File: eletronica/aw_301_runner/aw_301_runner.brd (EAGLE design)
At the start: 100 x 80 mm, 9 parts, among them IC1 AT90S2313P, Q1 4 Mhz

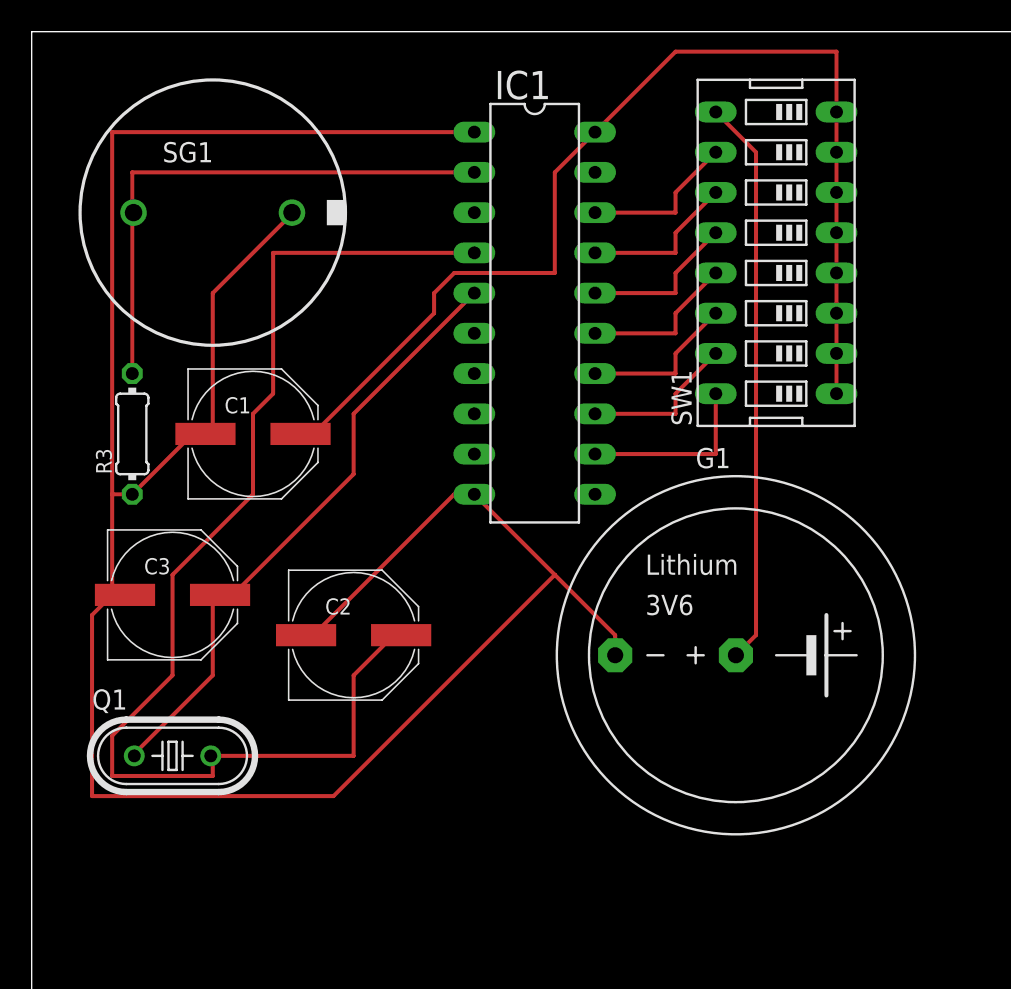
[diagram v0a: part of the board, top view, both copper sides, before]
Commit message: 
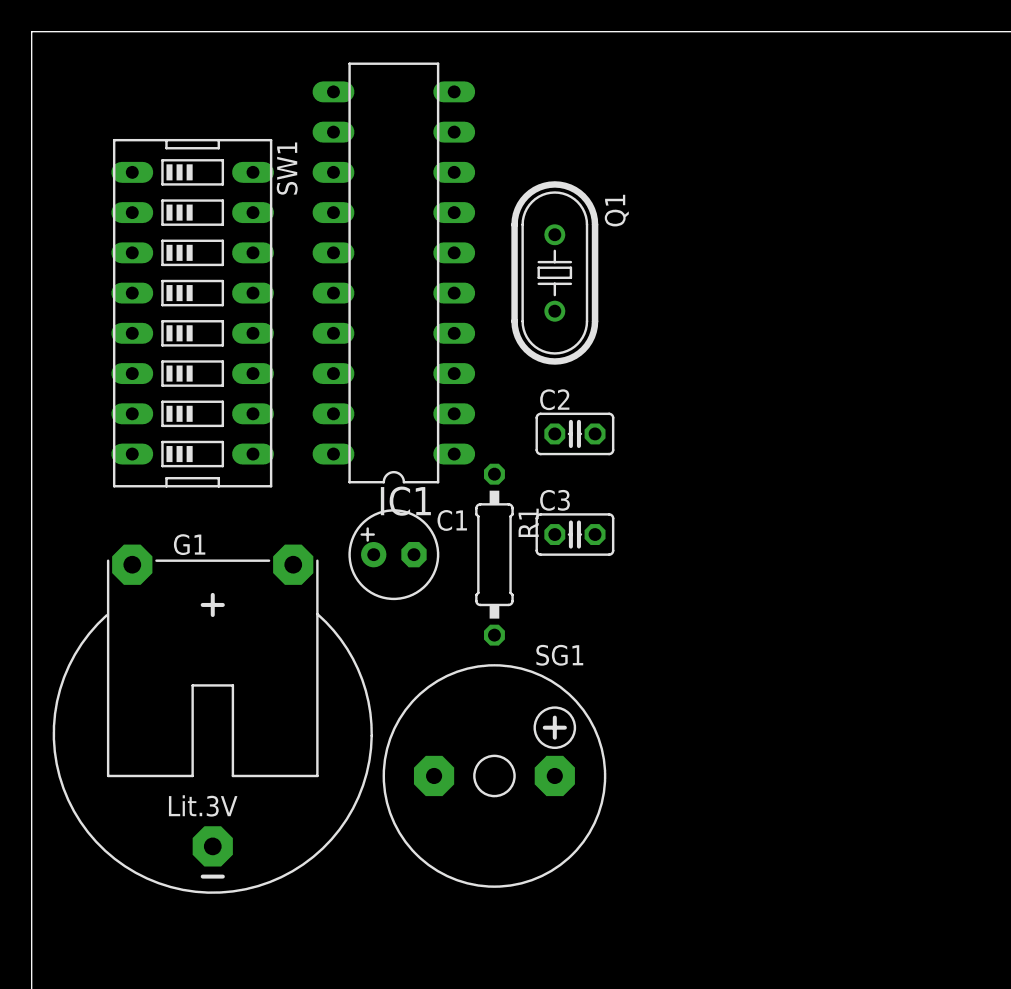
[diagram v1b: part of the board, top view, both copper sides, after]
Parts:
- removed R3: 1M, resistor:0204/7
- added R1: 1M, rcl:0207/10
- C1: device resistor:PANASONIC_E -> resistor:E2,5-6
- C2, C3: device resistor:PANASONIC_E -> rcl:C025-025X050
- G1: value SL340P -> CR2032H; device battery:SL-340/P3.6V -> battery:CR2032H
- Q1: value 4 Mhz -> (none); device crystal:HC49U-V -> crystal:HC49U70
- SG1: value EFBAA40D101 -> F/CM12P; device buzzer:EFBAA40D101 -> buzzer:F/CM12P
- moved SG1 39.8 mm to (29.2, 33.0)
- moved Q1 38.9 mm to (33.0, 64.8), turned to 270 degrees
- moved SW1 37.0 mm to (10.2, 62.2), turned to 270 degrees
- moved G1 33.4 mm to (11.4, 35.6)
- moved C3 25.7 mm to (34.3, 48.3)
- moved C2 18.9 mm to (34.3, 54.6)
- moved C1 11.7 mm to (22.9, 47.0)
- moved IC1 9.25 mm to (22.9, 64.8), turned to 90 degrees
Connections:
- net N$2: now also C2.2; no longer C2.+
- net N$3: now also C3.2; no longer C3.+
- net N$6: now also R1.2, SG1.+; no longer R3.2, SG1.1
- net N$7: now also C2.1, C3.1, R1.1, SG1.-; no longer C2.-, C3.-, R3.1, SG1.2
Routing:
- net N$7: track 153.3 -> 0.00 mm
- net N$2: track 75.7 -> 0.00 mm
- net N$5: track 69.9 -> 0.00 mm
- net N$3: track 39.0 -> 0.00 mm
- net N$1: track 35.9 -> 0.00 mm
- net N$6: track 34.4 -> 0.00 mm
- net N$8: track 11.4 -> 0.00 mm
- net N$14: track 9.94 -> 0.00 mm
- net N$12: track 9.94 -> 0.00 mm
- net N$9: track 9.94 -> 0.00 mm
- net N$11: track 9.94 -> 0.00 mm
- net N$10: track 9.94 -> 0.00 mm
- net N$13: track 9.94 -> 0.00 mm

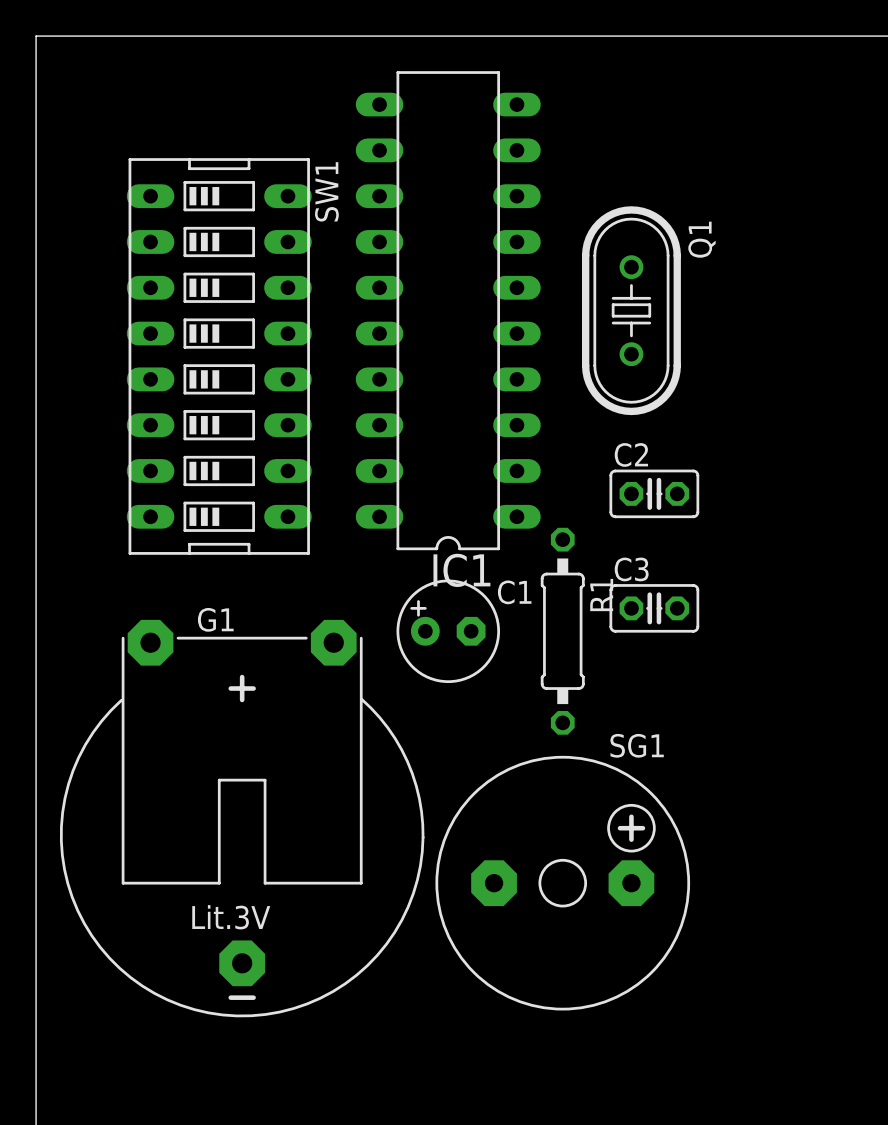
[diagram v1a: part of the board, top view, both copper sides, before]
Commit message: 
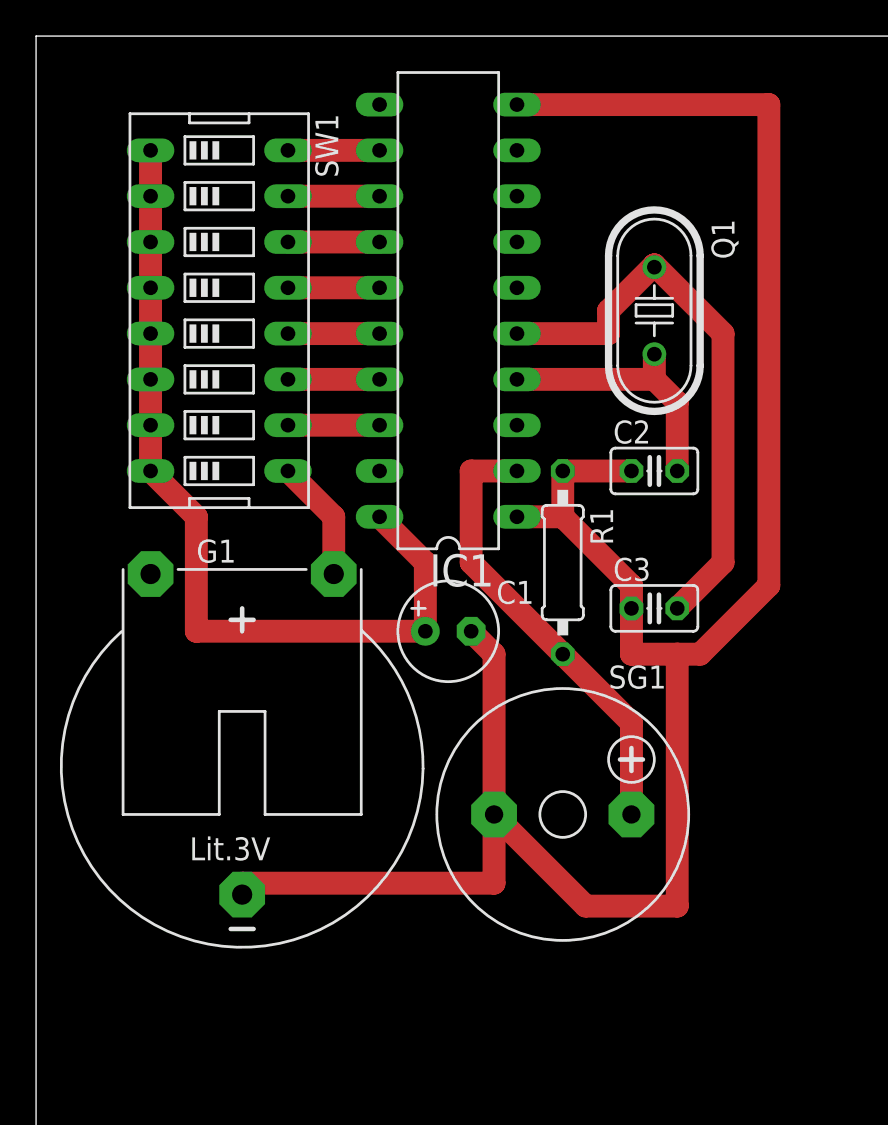
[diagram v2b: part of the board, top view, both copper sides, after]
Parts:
- moved G1 3.81 mm to (11.4, 39.4)
- moved R1 3.81 mm to (29.2, 50.8)
- moved SG1 3.81 mm to (29.2, 36.8)
- moved SW1 2.54 mm to (10.2, 64.8)
- moved C2 1.27 mm to (34.3, 55.9)
- moved Q1 1.27 mm to (34.3, 64.8)
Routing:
- net N$7: track 0.00 -> 123.3 mm
- net N$5: track 0.00 -> 47.8 mm
- net N$3: track 0.00 -> 31.7 mm
- net N$6: track 0.00 -> 25.3 mm
- net N$2: track 0.00 -> 14.6 mm
- net N$1: track 0.00 -> 6.77 mm
- net N$9: track 0.00 -> 5.08 mm
- net N$8: track 0.00 -> 5.08 mm
- net N$14: track 0.00 -> 5.08 mm
- net N$13: track 0.00 -> 5.08 mm
- net N$12: track 0.00 -> 5.08 mm
- net N$11: track 0.00 -> 5.08 mm
- net N$10: track 0.00 -> 5.08 mm

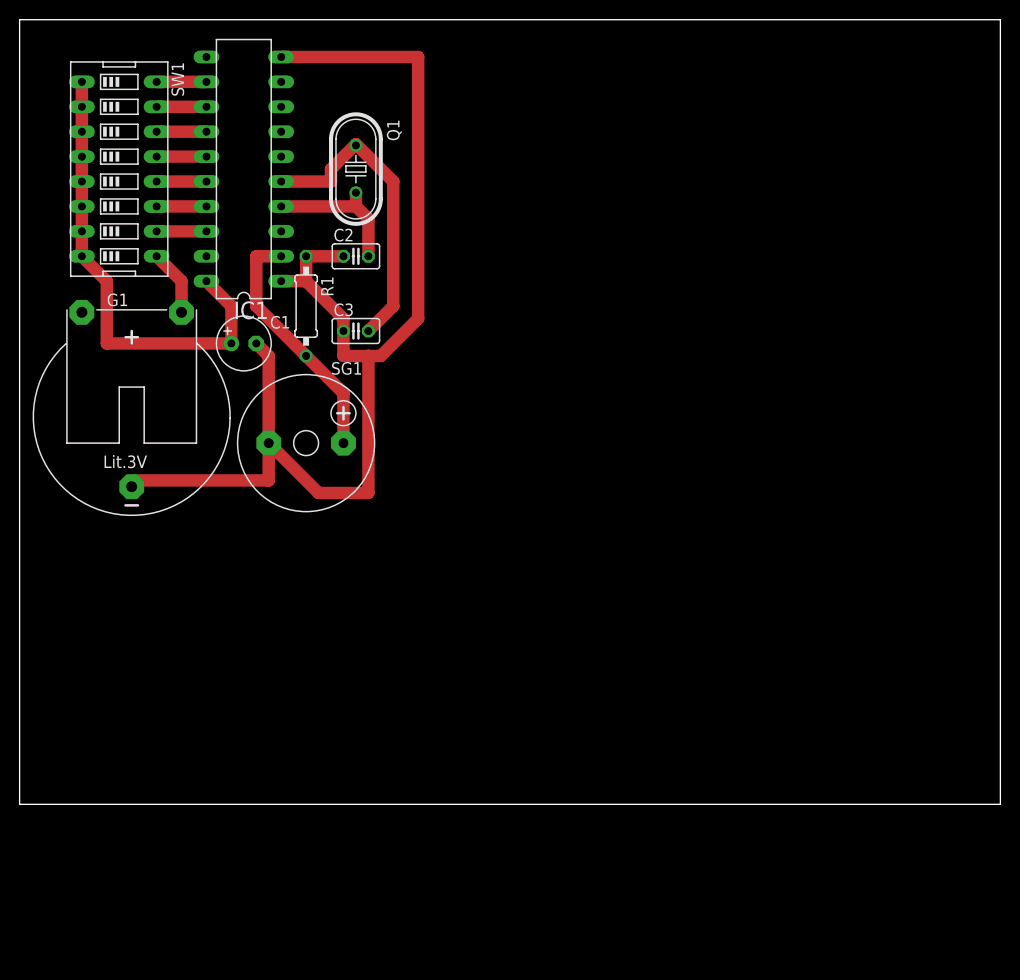
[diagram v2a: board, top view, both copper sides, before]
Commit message: 
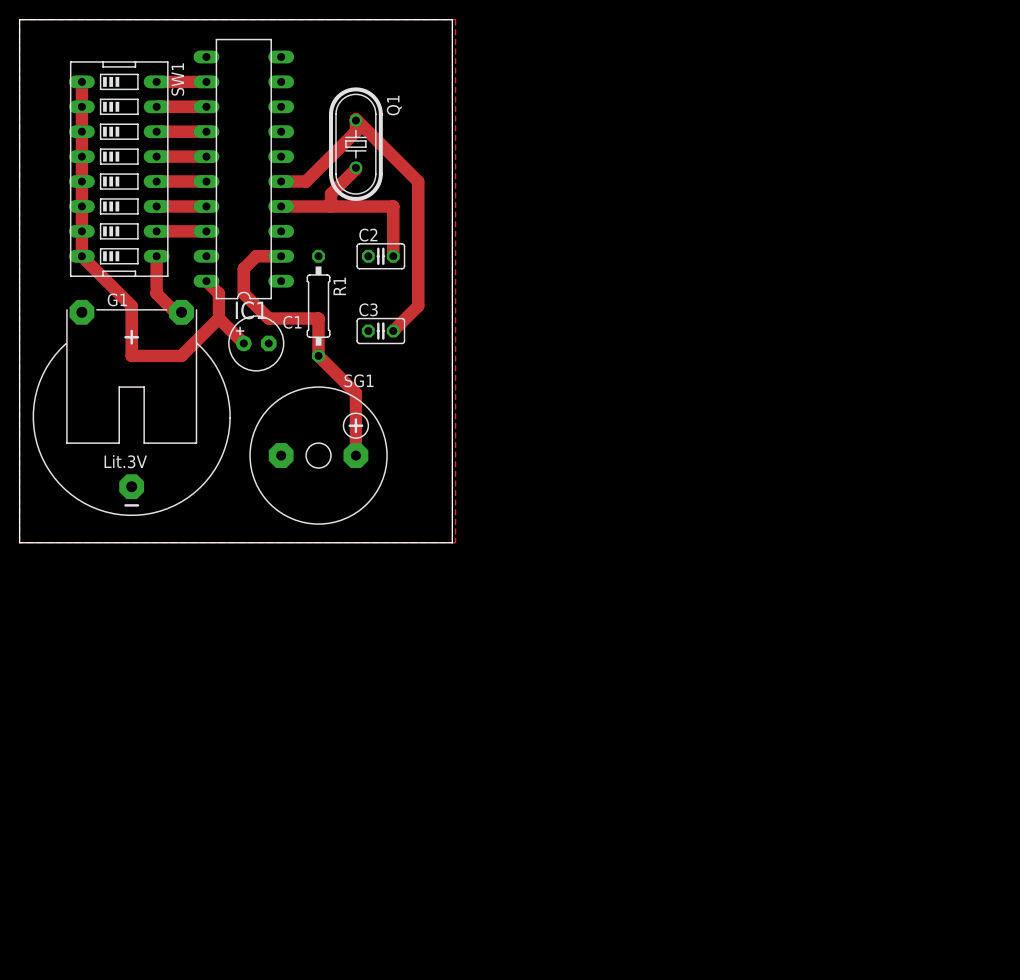
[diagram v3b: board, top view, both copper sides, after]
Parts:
- IC1: value AT90S2313P -> ATTINY2313V
- Q1: value (none) -> 4 Mhz
- moved Q1 2.54 mm to (34.3, 67.3)
- moved C2 2.54 mm to (36.8, 55.9)
- moved C3 2.54 mm to (36.8, 48.3)
- moved SG1 1.80 mm to (30.5, 35.6)
- moved C1 1.27 mm to (24.1, 47.0)
- moved R1 1.27 mm to (30.5, 50.8)
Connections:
- net N$5 renamed VCC
- net N$7 renamed GND
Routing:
- net GND: track 123.3 -> 0.00 mm
- net N$2: track 14.6 -> 21.5 mm
- net N$6: track 25.3 -> 31.1 mm
- net N$3: track 31.7 -> 36.3 mm
- net N$1: track 6.77 -> 8.04 mm
- net VCC: track 47.8 -> 48.4 mm
- added copper zone on layer 1, net GND
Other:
- board size 100 x 80 mm -> 44.1 x 53.3 mm
